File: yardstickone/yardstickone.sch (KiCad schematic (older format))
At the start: 69 parts, among them J1 USB-DEVICE, P1 CONN_02X07, P2 SMA-EDGE, P3 RESET_N, P4 DD, P5 DC, P6 3V3, P7 GND, T1 BALUN, U1 CC1111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

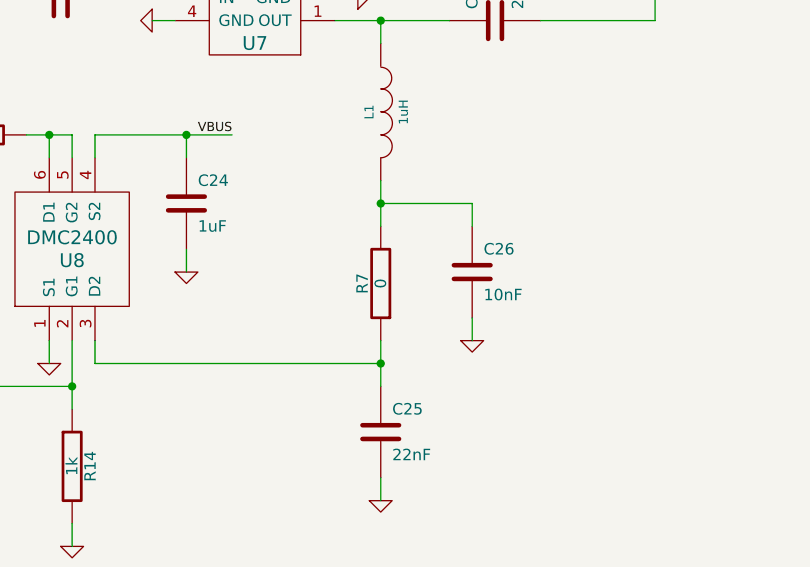
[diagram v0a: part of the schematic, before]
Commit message: replace 0 ohm R7 with PCB trace
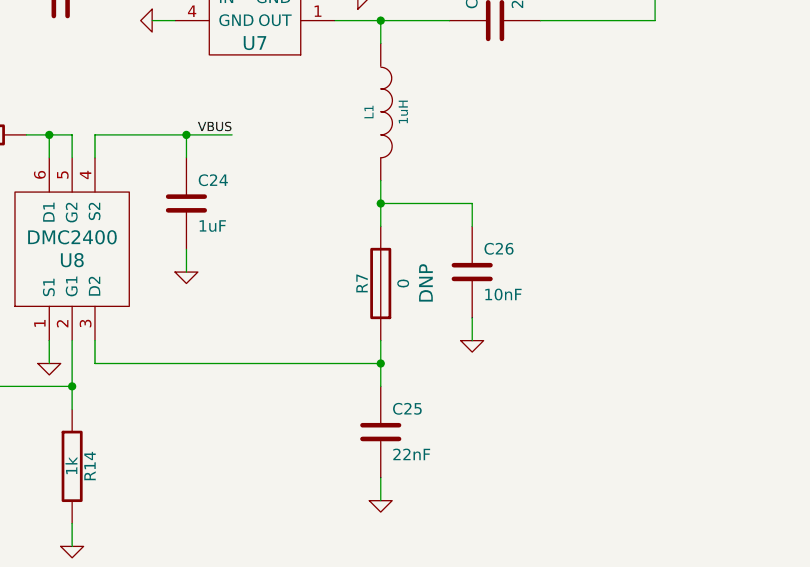
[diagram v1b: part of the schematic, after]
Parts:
- removed R7: 0, cc1111-legacy:GSG-0402, symbol R
- added R7: 0, cc1111-legacy:GSG-0603-SHORT-10MIL, symbol R-SHORTED
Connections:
- net at C26.1, L1.2: now also R7.2
- net at C25.1, U8.3 (D2): now also R7.1
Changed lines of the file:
@@
 	7800 9300 7800 9600
-$Comp
-L R R7
-U 1 1 5494B37F
-P 11750 7550
-F 0 "R7" V 11830 7550 50  0000 C CNN
-F 1 "0" V 11750 7550 50  0000 C CNN
-F 2 "cc1111-legacy:GSG-0402" H 11750 7550 60  0001 C CNN
-F 3 "" H 11750 7550 60  0001 C CNN
-	1    11750 7550
-	-1   0    0    1
-$EndComp
 $Comp
 L BGA420 U4
@@
 Wire Wire Line
 	14700 5150 14900 5150
+$Comp
+L R-SHORTED R7
+U 1 1 54E4279D
+P 11750 7550
+F 0 "R7" V 11830 7550 50  0000 C CNN
+F 1 "0" V 11650 7550 50  0000 C CNN
+F 2 "cc1111-legacy:GSG-0603-SHORT-10MIL" H 11750 7550 60  0001 C CNN
+F 3 "" H 11750 7550 60  0001 C CNN
+F 4 "DNP" V 11550 7550 60  0000 C CNN "Note"
+	1    11750 7550
+	-1   0    0    1
+$EndComp
 $EndSCHEMATC

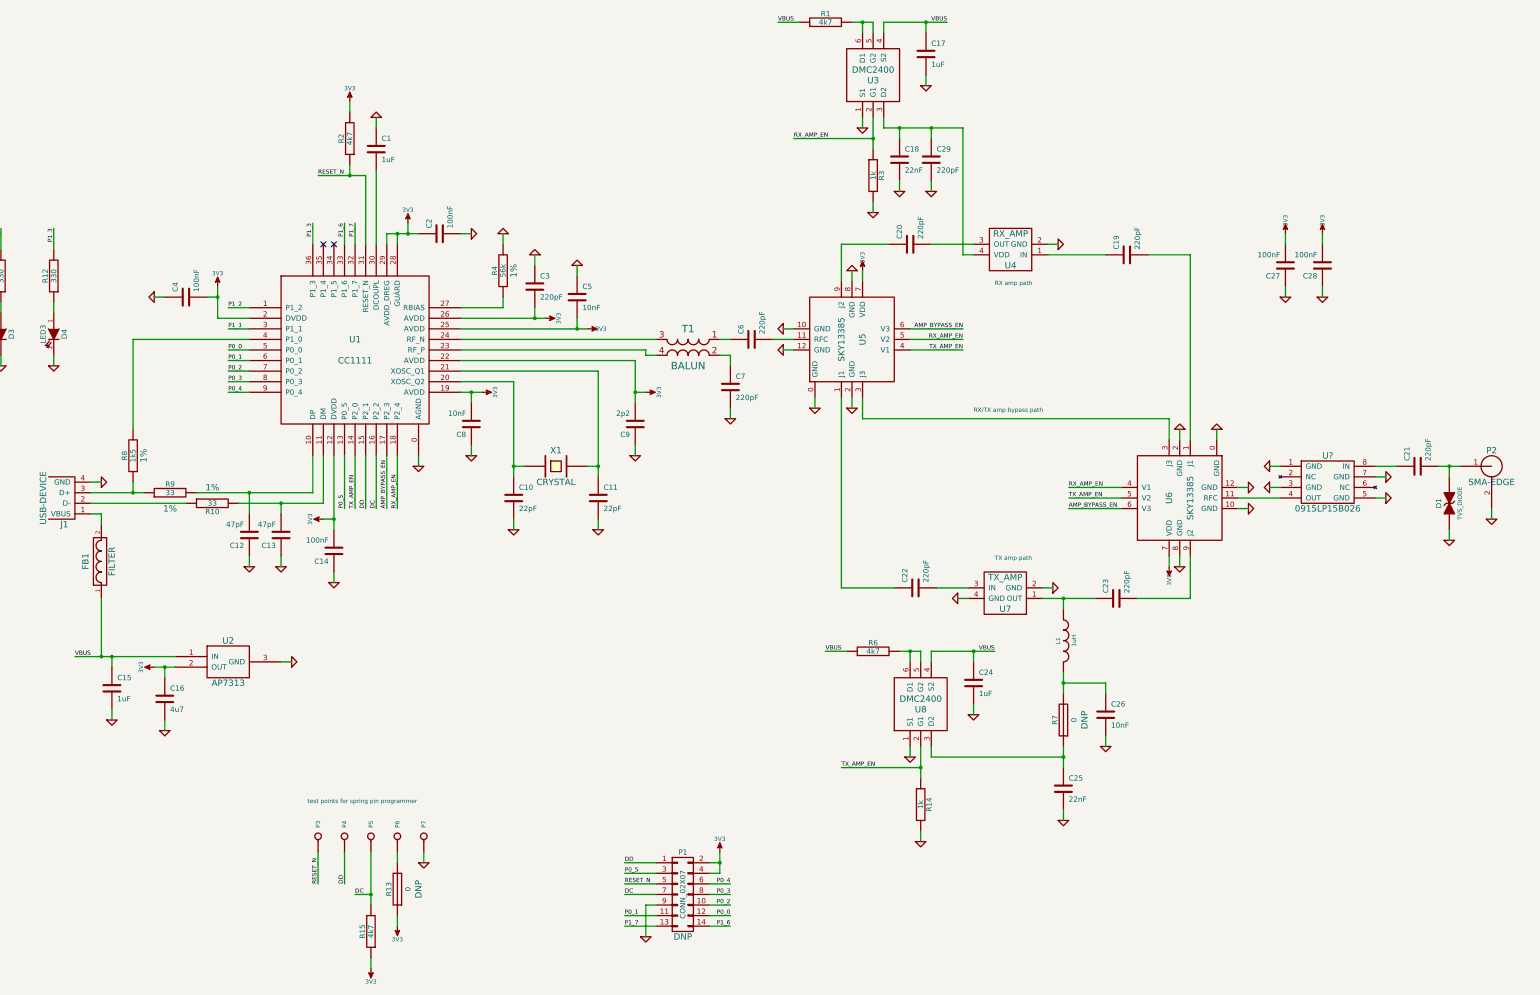
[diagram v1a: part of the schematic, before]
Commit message: added antenna port power control
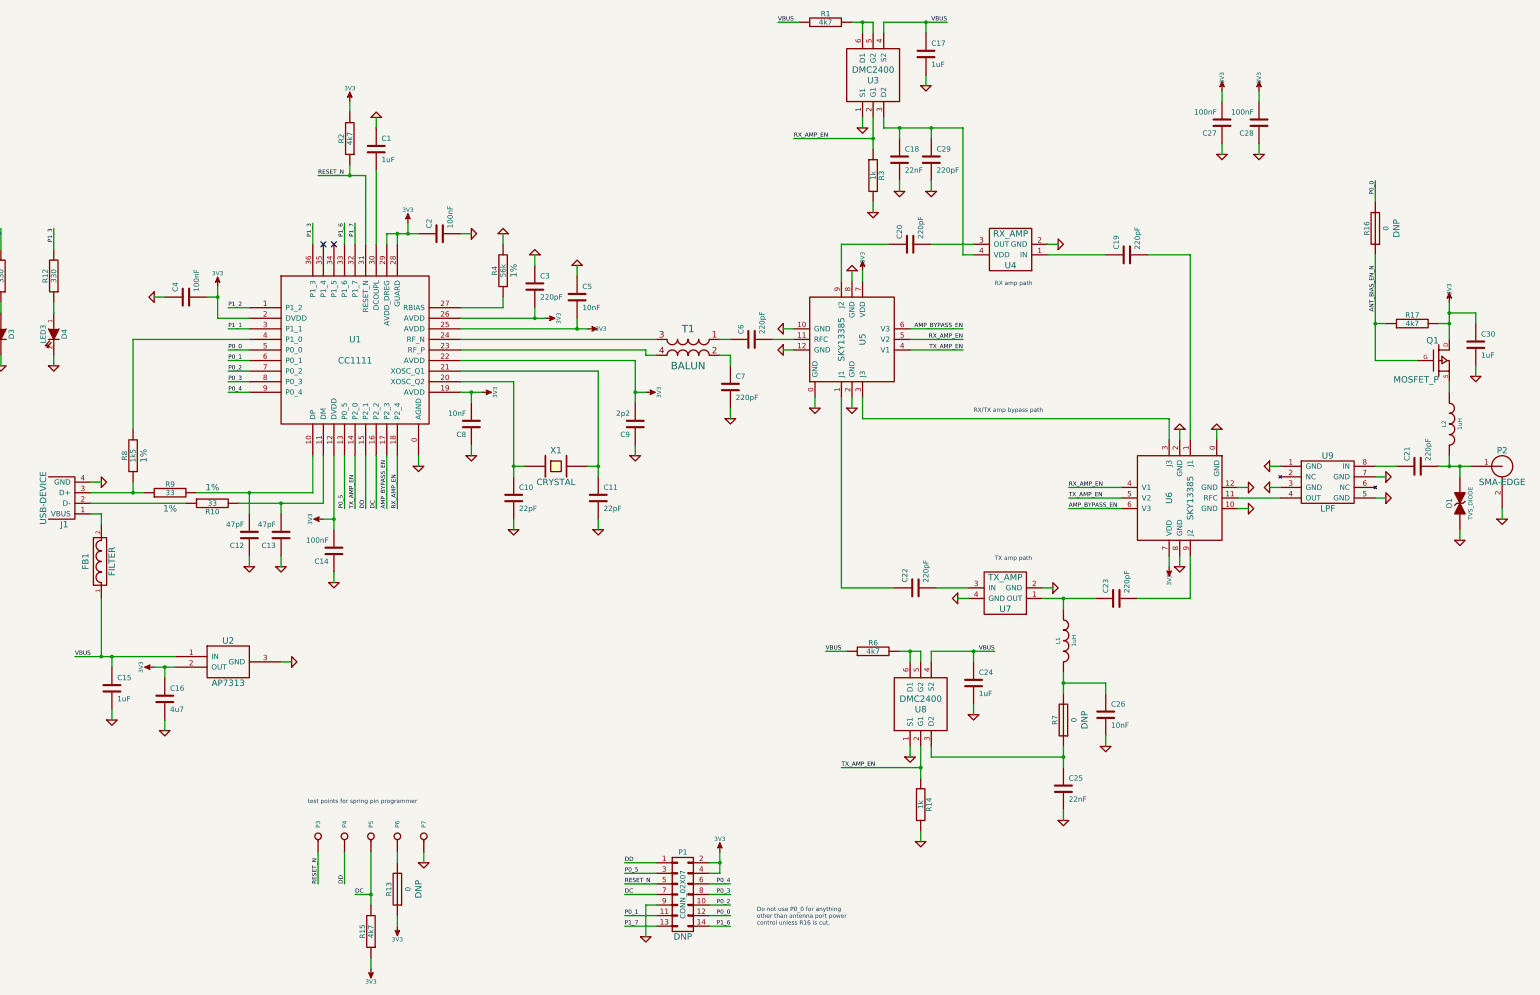
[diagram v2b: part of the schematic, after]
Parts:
- added C30: 1uF, cc1111-legacy:GSG-0603, symbol C
- added L2: 1uH, cc1111-legacy:GSG-0603, symbol INDUCTOR
- added Q1: MOSFET_P, symbol MOSFET_P
- added R16: 0, cc1111-legacy:GSG-0603-SHORT-10MIL, symbol R-SHORTED
- added R17: 4k7, cc1111-legacy:GSG-0402, symbol R
- U9: renamed from U?; value 0915LP15B026 -> LPF; Description (none) -> FILTER LOWPASS GSM/CDMA 915MHZ; Manufacturer (none) -> Johanson Technology; Part Number (none) -> 0915LP15B026
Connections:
- net 3V3: now also C30.1, Q1.D, R17.2
- net GND: now also C30.2
- net P0_0: now also R16.2
- net at C21.2, D1.2 (K), P2.1 (RF): now also L2.2
- new net: L2.1, Q1.S
- new net ANT_BIAS_EN_N: Q1.G, R16.1, R17.1
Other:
- note added: "Do not use P0_0 for anything\nother than antenna port power\ncontrol unless R16 is cut."
- moved on the sheet: C27, C28, D1, P2

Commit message: saved schematic
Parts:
- Q1: footprint (none) -> sot23:SOT23-3GDS
- U9: footprint (none) -> filter:0915LP15B026

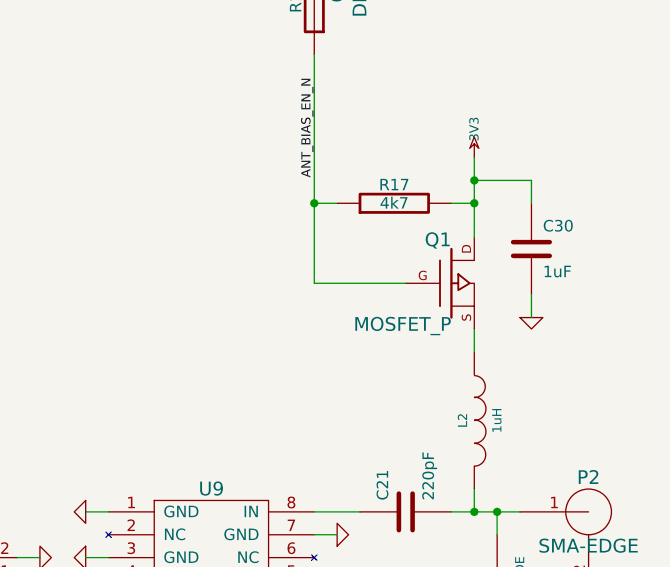
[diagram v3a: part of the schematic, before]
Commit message: reversed MOSFET drain and source
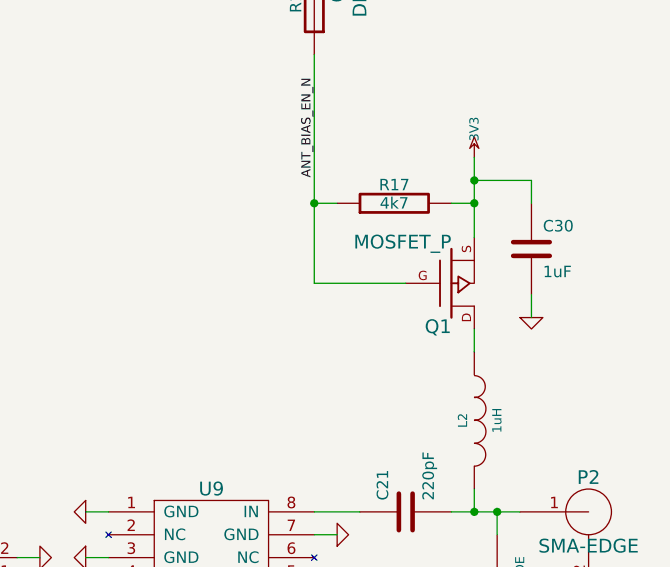
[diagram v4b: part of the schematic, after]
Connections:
- net 3V3: now also Q1.S; no longer Q1.D
- net at L2.1: now also Q1.D; no longer Q1.S
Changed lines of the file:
@@
 F 6 "MOSFET P-CH 50V 130MA SOT-23" H 15300 4150 60  0001 C CNN "Description"
 	1    15300 4150
-	1    0    0    -1
+	1    0    0    1
 $EndComp
 $Comp

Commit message: LED part selection
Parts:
- D2: Description LED CHIPLED 570NM GREEN 0603 SMD -> LED 1.6X0.8MM 568NM GRN CLR SMD; Manufacturer OSRAM -> Kingbright; Part Number LG Q971-KN-1 -> APT1608SGC
- D3: Description LED CHIPLED 570NM GREEN 0603 SMD -> LED 1.6X0.8MM 625NM RED CLR SMD; Manufacturer OSRAM -> Kingbright; Part Number LG Q971-KN-1 -> APT1608EC
- D4: Description LED CHIPLED 570NM GREEN 0603 SMD -> LED 1.6X0.8MM 588NM YLW CLR SMD; Manufacturer OSRAM -> Kingbright; Part Number LG Q971-KN-1 -> APT1608YC
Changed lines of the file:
@@
 F 2 "cc1111-legacy:GSG-0603D" H 2200 3900 60  0001 C CNN
 F 3 "" H 2200 3900 60  0001 C CNN
-F 4 "OSRAM" H 2200 3900 60  0001 C CNN "Manufacturer"
-F 5 "LG Q971-KN-1" H 2200 3900 60  0001 C CNN "Part Number"
-F 6 "LED CHIPLED 570NM GREEN 0603 SMD" H 2200 3900 60  0001 C CNN "Description"
+F 4 "Kingbright" H 2200 3900 60  0001 C CNN "Manufacturer"
+F 5 "APT1608YC" H 2200 3900 60  0001 C CNN "Part Number"
+F 6 "LED 1.6X0.8MM 588NM YLW CLR SMD" H 2200 3900 60  0001 C CNN "Description"
 	1    2200 3900
 	0    1    1    0
@@
 F 2 "cc1111-legacy:GSG-0603D" H 1700 3900 60  0001 C CNN
 F 3 "" H 1700 3900 60  0001 C CNN
-F 4 "OSRAM" H 1700 3900 60  0001 C CNN "Manufacturer"
-F 5 "LG Q971-KN-1" H 1700 3900 60  0001 C CNN "Part Number"
-F 6 "LED CHIPLED 570NM GREEN 0603 SMD" H 1700 3900 60  0001 C CNN "Description"
+F 4 "Kingbright" H 1700 3900 60  0001 C CNN "Manufacturer"
+F 5 "APT1608EC" H 1700 3900 60  0001 C CNN "Part Number"
+F 6 "LED 1.6X0.8MM 625NM RED CLR SMD" H 1700 3900 60  0001 C CNN "Description"
 	1    1700 3900
 	0    1    1    0
@@
 F 2 "cc1111-legacy:GSG-0603D" H 1200 3900 60  0001 C CNN
 F 3 "" H 1200 3900 60  0001 C CNN
-F 4 "OSRAM" H 1200 3900 60  0001 C CNN "Manufacturer"
-F 5 "LG Q971-KN-1" H 1200 3900 60  0001 C CNN "Part Number"
-F 6 "LED CHIPLED 570NM GREEN 0603 SMD" H 1200 3900 60  0001 C CNN "Description"
+F 4 "Kingbright" H 1200 3900 60  0001 C CNN "Manufacturer"
+F 5 "APT1608SGC" H 1200 3900 60  0001 C CNN "Part Number"
+F 6 "LED 1.6X0.8MM 568NM GRN CLR SMD" H 1200 3900 60  0001 C CNN "Description"
 	1    1200 3900
 	0    1    1    0

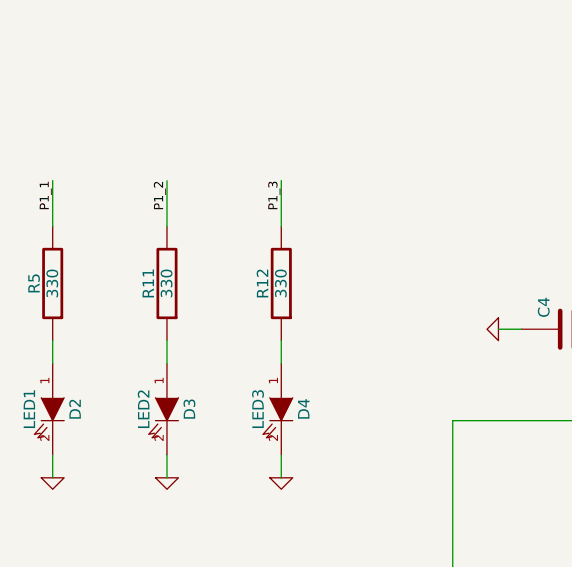
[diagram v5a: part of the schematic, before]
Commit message: changed R11 value to tone down red LED2
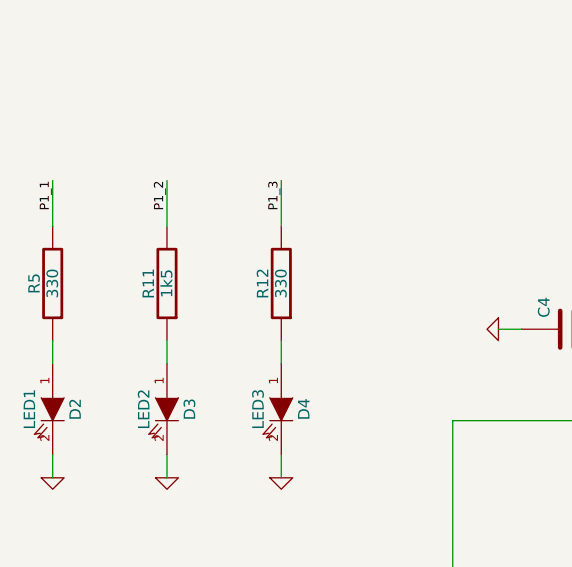
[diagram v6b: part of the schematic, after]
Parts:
- R11: value 330 -> 1k5; Description RES 330 OHM 1/10W 5% 0603 SMD -> RES 1.50K OHM 1/10W 1% 0603 SMD; Manufacturer Stackpole -> Rohm; Part Number RMCF0603JT330R -> MCR03ERTF1501
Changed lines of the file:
@@
-$EndComp
-$Comp
-L R R11
-U 1 1 504CFE39
-P 1700 3350
-F 0 "R11" V 1780 3350 50  0000 C CNN
-F 1 "330" V 1700 3350 50  0000 C CNN
-F 2 "cc1111-legacy:GSG-0603" H 1700 3350 60  0001 C CNN
-F 3 "" H 1700 3350 60  0001 C CNN
-F 4 "Stackpole" H 1700 3350 60  0001 C CNN "Manufacturer"
-F 5 "RMCF0603JT330R" H 1700 3350 60  0001 C CNN "Part Number"
-F 6 "RES 330 OHM 1/10W 5% 0603 SMD" H 1700 3350 60  0001 C CNN "Description"
-	1    1700 3350
-	-1   0    0    1
 $EndComp
 $Comp
@@
 Text Notes 8850 9500 0    40   ~ 0
 Do not use P0_0 for anything\nother than antenna port power\ncontrol unless R16 is cut.
+$Comp
+L R R11
+U 1 1 559B82A0
+P 1700 3350
+F 0 "R11" V 1780 3350 50  0000 C CNN
+F 1 "1k5" V 1700 3350 50  0000 C CNN
+F 2 "cc1111-legacy:GSG-0603" H 1700 3350 60  0001 C CNN
+F 3 "" H 1700 3350 60  0001 C CNN
+F 4 "Rohm" H 1700 3350 60  0001 C CNN "Manufacturer"
+F 5 "MCR03ERTF1501" H 1700 3350 60  0001 C CNN "Part Number"
+F 6 "RES 1.50K OHM 1/10W 1% 0603 SMD" H 1700 3350 60  0001 C CNN "Description"
+	1    1700 3350
+	-1   0    0    1
+$EndComp
 $EndSCHEMATC

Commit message: renumbered confusing diode reference numbers
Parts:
- renumbered D2 to D1, D3 to D2, D4 to D3, D1 to D4
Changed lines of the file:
@@
 $EndComp
 $Comp
-L LED D4
+L LED D3
 U 1 1 504CFE70
 P 2200 3900
-F 0 "D4" H 2200 4000 50  0000 C CNN
+F 0 "D3" H 2200 4000 50  0000 C CNN
 F 1 "LED3" H 2200 3800 50  0000 C CNN
 F 2 "cc1111-legacy:GSG-0603D" H 2200 3900 60  0001 C CNN
@@
 $EndComp
 $Comp
-L LED D3
+L LED D2
 U 1 1 504CFE38
 P 1700 3900
-F 0 "D3" H 1700 4000 50  0000 C CNN
+F 0 "D2" H 1700 4000 50  0000 C CNN
 F 1 "LED2" H 1700 3800 50  0000 C CNN
 F 2 "cc1111-legacy:GSG-0603D" H 1700 3900 60  0001 C CNN
@@
 $EndComp
 $Comp
-L GSG-DIODE-TVS-BI D1
+L GSG-DIODE-TVS-BI D4
 U 1 1 504CFCBE
 P 15500 5500
-F 0 "D1" H 15500 5600 50  0000 C CNN
+F 0 "D4" H 15500 5600 50  0000 C CNN
 F 1 "TVS_DIODE" H 15500 5400 40  0000 C CNN
 F 2 "cc1111-legacy:GSG-0402" H 15500 5500 60  0001 C CNN
@@
 $EndComp
 $Comp
-L LED D2
+L LED D1
 U 1 1 504CF0C2
 P 1200 3900
-F 0 "D2" H 1200 4000 50  0000 C CNN
+F 0 "D1" H 1200 4000 50  0000 C CNN
 F 1 "LED1" H 1200 3800 50  0000 C CNN
 F 2 "cc1111-legacy:GSG-0603D" H 1200 3900 60  0001 C CNN

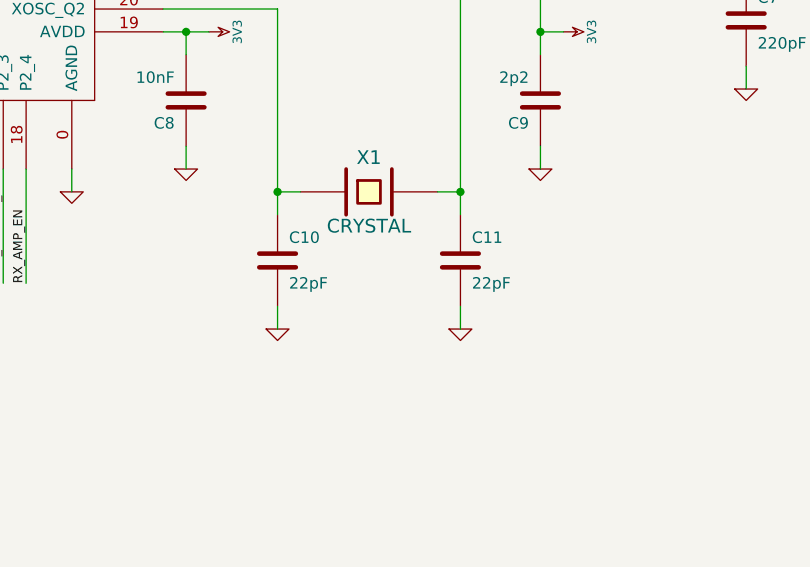
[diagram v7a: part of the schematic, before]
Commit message: replaced crystal load caps with 30 pF
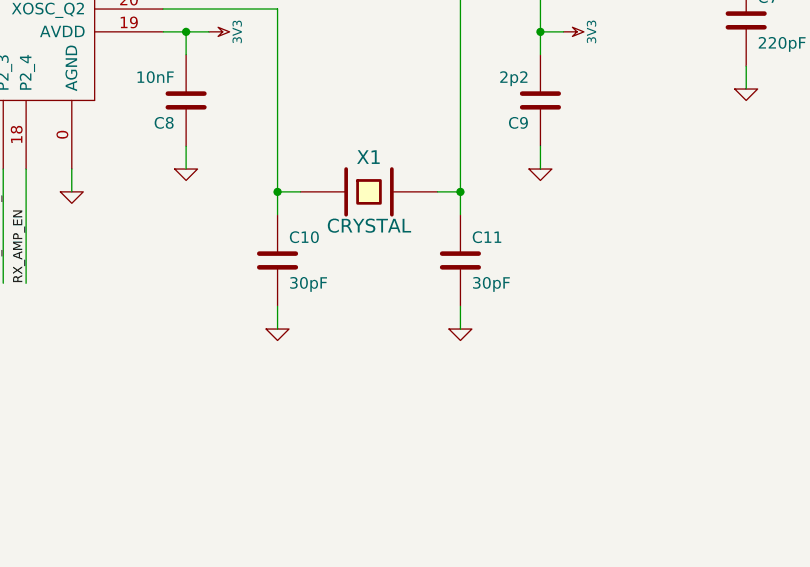
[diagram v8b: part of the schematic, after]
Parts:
- C10, C11: value 22pF -> 30pF; Description CAP CER 22PF 50V 5% NP0 0402 -> CAP CER 30PF 50V 5% NP0 0402; Part Number GRM1555C1H220JA01D -> GRM1555C1H300JA01D
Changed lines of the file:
@@
 P 7350 5450
 F 0 "C11" H 7400 5550 50  0000 L CNN
-F 1 "22pF" H 7400 5350 50  0000 L CNN
+F 1 "30pF" H 7400 5350 50  0000 L CNN
 F 2 "cc1111-legacy:GSG-0402" H 7350 5450 60  0001 C CNN
 F 3 "" H 7350 5450 60  0001 C CNN
 F 4 "Murata" H 7350 5450 60  0001 C CNN "Manufacturer"
-F 5 "GRM1555C1H220JA01D" H 7350 5450 60  0001 C CNN "Part Number"
-F 6 "CAP CER 22PF 50V 5% NP0 0402" H 7350 5450 60  0001 C CNN "Description"
+F 5 "GRM1555C1H300JA01D" H 7350 5450 60  0001 C CNN "Part Number"
+F 6 "CAP CER 30PF 50V 5% NP0 0402" H 7350 5450 60  0001 C CNN "Description"
 	1    7350 5450
 	1    0    0    -1
@@
 P 6550 5450
 F 0 "C10" H 6600 5550 50  0000 L CNN
-F 1 "22pF" H 6600 5350 50  0000 L CNN
+F 1 "30pF" H 6600 5350 50  0000 L CNN
 F 2 "cc1111-legacy:GSG-0402" H 6550 5450 60  0001 C CNN
 F 3 "" H 6550 5450 60  0001 C CNN
 F 4 "Murata" H 6550 5450 60  0001 C CNN "Manufacturer"
-F 5 "GRM1555C1H220JA01D" H 6550 5450 60  0001 C CNN "Part Number"
-F 6 "CAP CER 22PF 50V 5% NP0 0402" H 6550 5450 60  0001 C CNN "Description"
+F 5 "GRM1555C1H300JA01D" H 6550 5450 60  0001 C CNN "Part Number"
+F 6 "CAP CER 30PF 50V 5% NP0 0402" H 6550 5450 60  0001 C CNN "Description"
 	1    6550 5450
 	1    0    0    -1
